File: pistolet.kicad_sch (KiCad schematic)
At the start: 8 parts, among them J16_Vers_Plastron_Dos_(CM)1 PinSocket_2x04_P2.54mm_Horizo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, J17_Emetteurs1 PinSocket_2x04_P2.54mm_Horizo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, J5 EMB_P3.81_1x04_VERTICAL

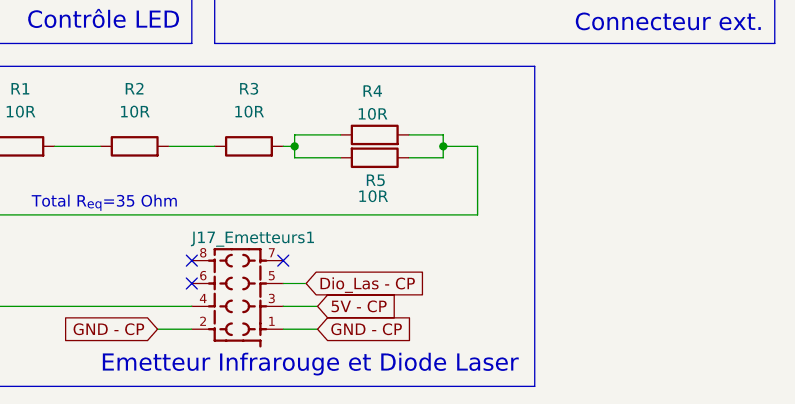
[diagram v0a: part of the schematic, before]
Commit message: changement de plan on oublie KiCad et on passe sur le nRF9160 SDK
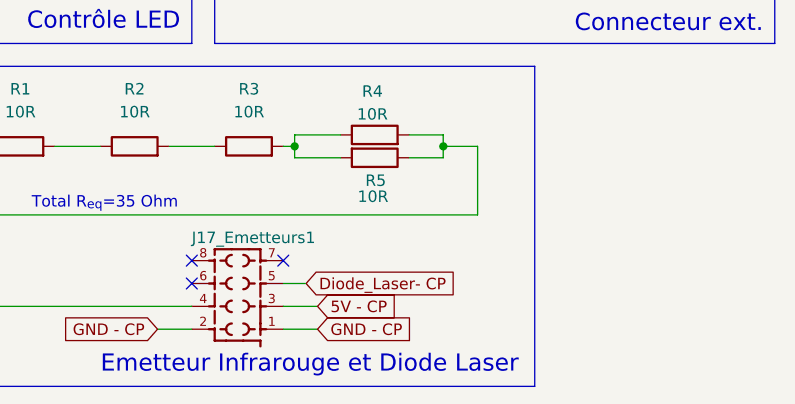
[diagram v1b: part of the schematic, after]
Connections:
- net Dio_Las - CP is gone; now on net Diode_Laser- CP: J17_Emetteurs1.5
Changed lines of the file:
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@@
 		)
 	)
-	(global_label "Dio_Las - CP"
+	(global_label "Diode_Laser- CP"
 		(shape input)
 		(at 74.93 76.2 0)
@@
 		)
 		(property "Intersheetrefs" "${INTERSHEET_REFS}"
-			(at 91.1594 76.2 0)
+			(at 94.3042 76.2 0)
 			(effects
 				(font
